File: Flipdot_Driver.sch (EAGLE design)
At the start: 27 parts

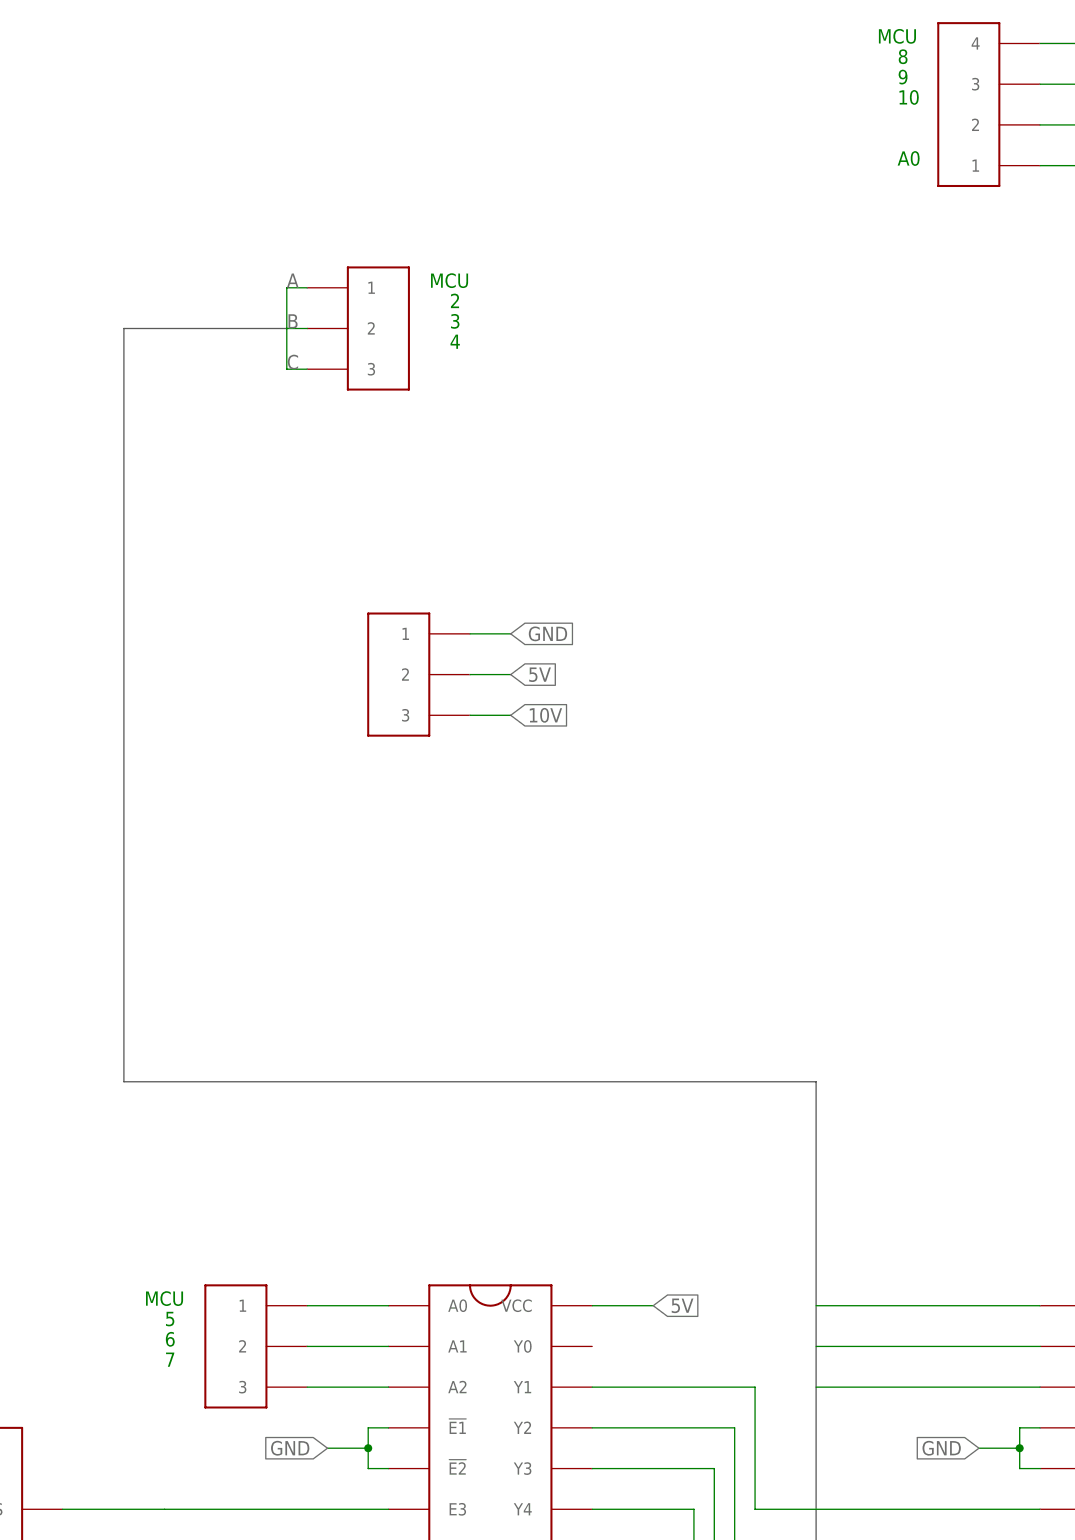
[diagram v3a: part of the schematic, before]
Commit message: Remapped outputs, replaced MCU
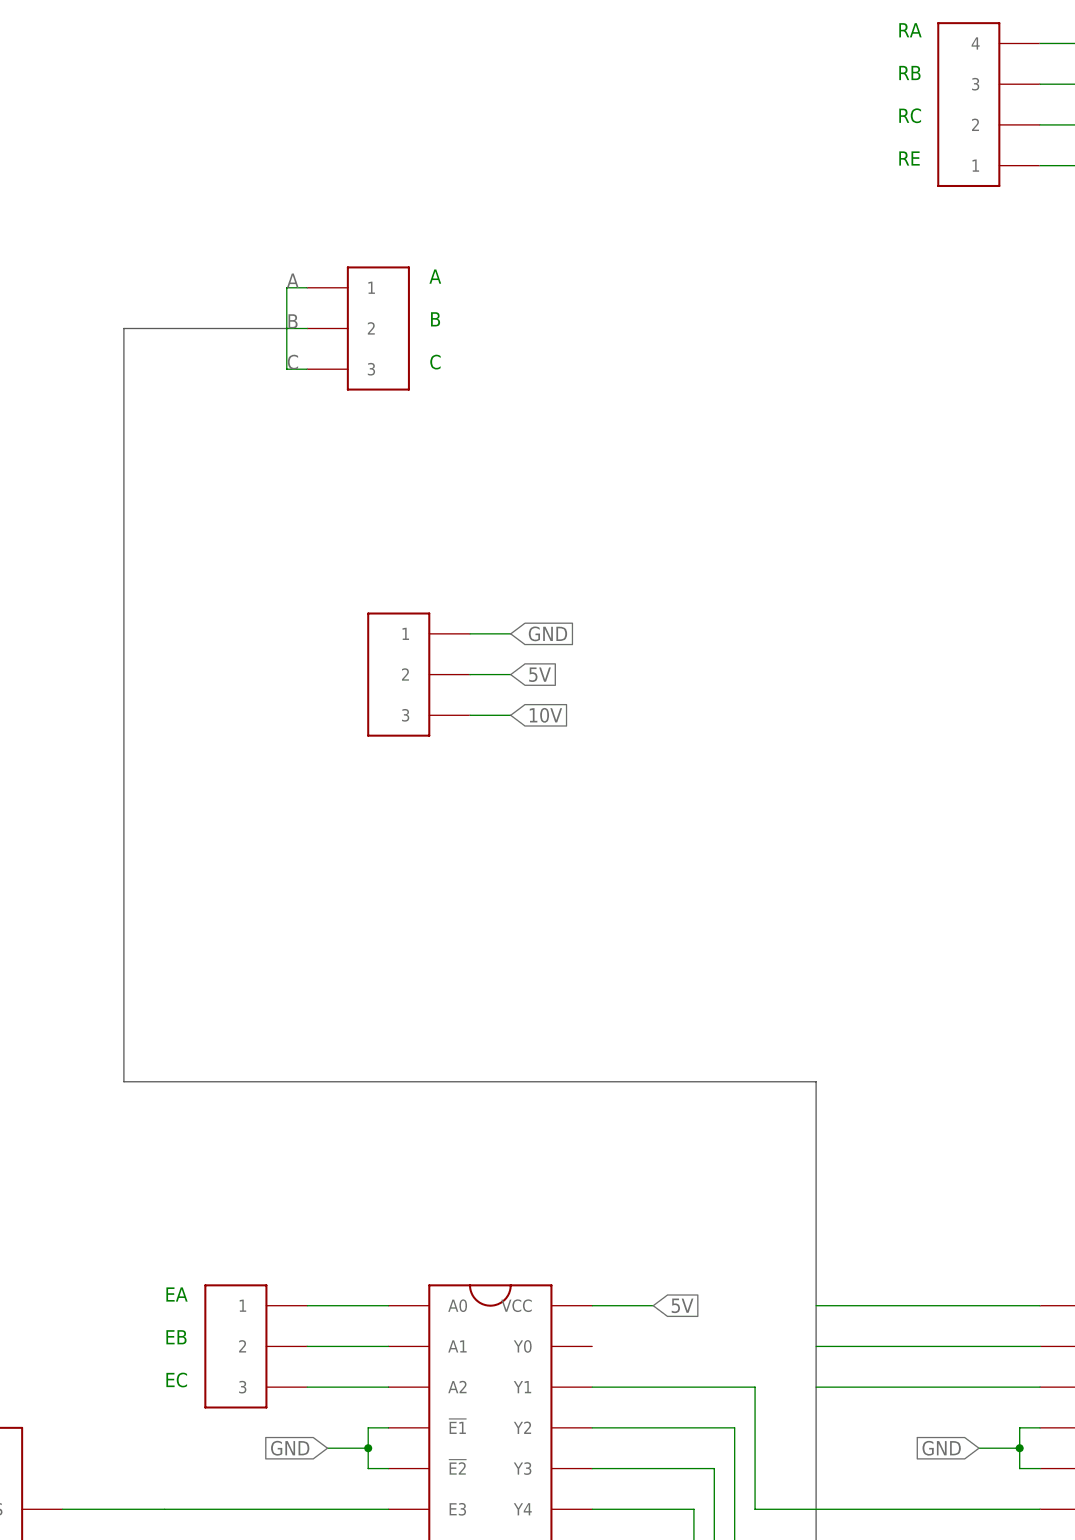
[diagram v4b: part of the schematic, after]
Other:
- note added: "A B C"
- note added: "EA EB EC"
- note added: "RA RB RC RE"
- note removed: "10"
- note removed: "2"
- note removed: "3"
- note removed: "4"
- note removed: "5"
- note removed: "6"
- note removed: "7"
- note removed: "8"
- note removed: "9"
- note removed: "A0"
- note removed: "MCU"
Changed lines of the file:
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@@
 <?xml version="1.0" encoding="utf-8"?>
 <!DOCTYPE eagle SYSTEM "eagle.dtd">
-<eagle version="9.2.2">
+<eagle version="9.3.2">
 <drawing>
 <settings>
@@
 <description>Driver circuit</description>
 <plain>
-<text x="-20.32" y="5.08" size="1.778" layer="91">2</text>
-<text x="-20.32" y="2.54" size="1.778" layer="91">3</text>
-<text x="-20.32" y="0" size="1.778" layer="91">4</text>
-<text x="-22.86" y="7.62" size="1.778" layer="91">MCU</text>
-<text x="-55.88" y="-121.92" size="1.778" layer="91">5</text>
-<text x="-55.88" y="-124.46" size="1.778" layer="91">6</text>
-<text x="-55.88" y="-127" size="1.778" layer="91">7</text>
-<text x="-58.42" y="-119.38" size="1.778" layer="91">MCU</text>
-<text x="35.56" y="35.56" size="1.778" layer="91">8</text>
-<text x="35.56" y="33.02" size="1.778" layer="91">9</text>
-<text x="35.56" y="30.48" size="1.778" layer="91">10</text>
-<text x="33.02" y="38.1" size="1.778" layer="91">MCU</text>
-<text x="35.56" y="22.86" size="1.778" layer="91">A0</text>
+<text x="-22.86" y="-2.54" size="1.778" layer="91">A
+B
+C</text>
+<text x="35.56" y="22.86" size="1.778" layer="91">RA
+RB
+RC
+RE</text>
+<text x="-55.88" y="-129.54" size="1.778" layer="91">EA
+EB
+EC</text>
 </plain>
 <instances>
@@
 </drawing>
 <compatibility>
+<note version="6.3" minversion="6.2.2" severity="warning">
+Since Version 6.2.2 text objects can contain more than one line,
+which will not be processed correctly with this version.
+</note>
 <note version="8.3" severity="warning">
 Since Version 8.3, EAGLE supports URNs for individual library
